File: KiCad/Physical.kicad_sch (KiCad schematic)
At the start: 11 parts, among them J159 Screw_Terminal_01x02, U106 AO3400A, U149 MT-0-103-F001-T000-RS+PJ, U181 AO3400A

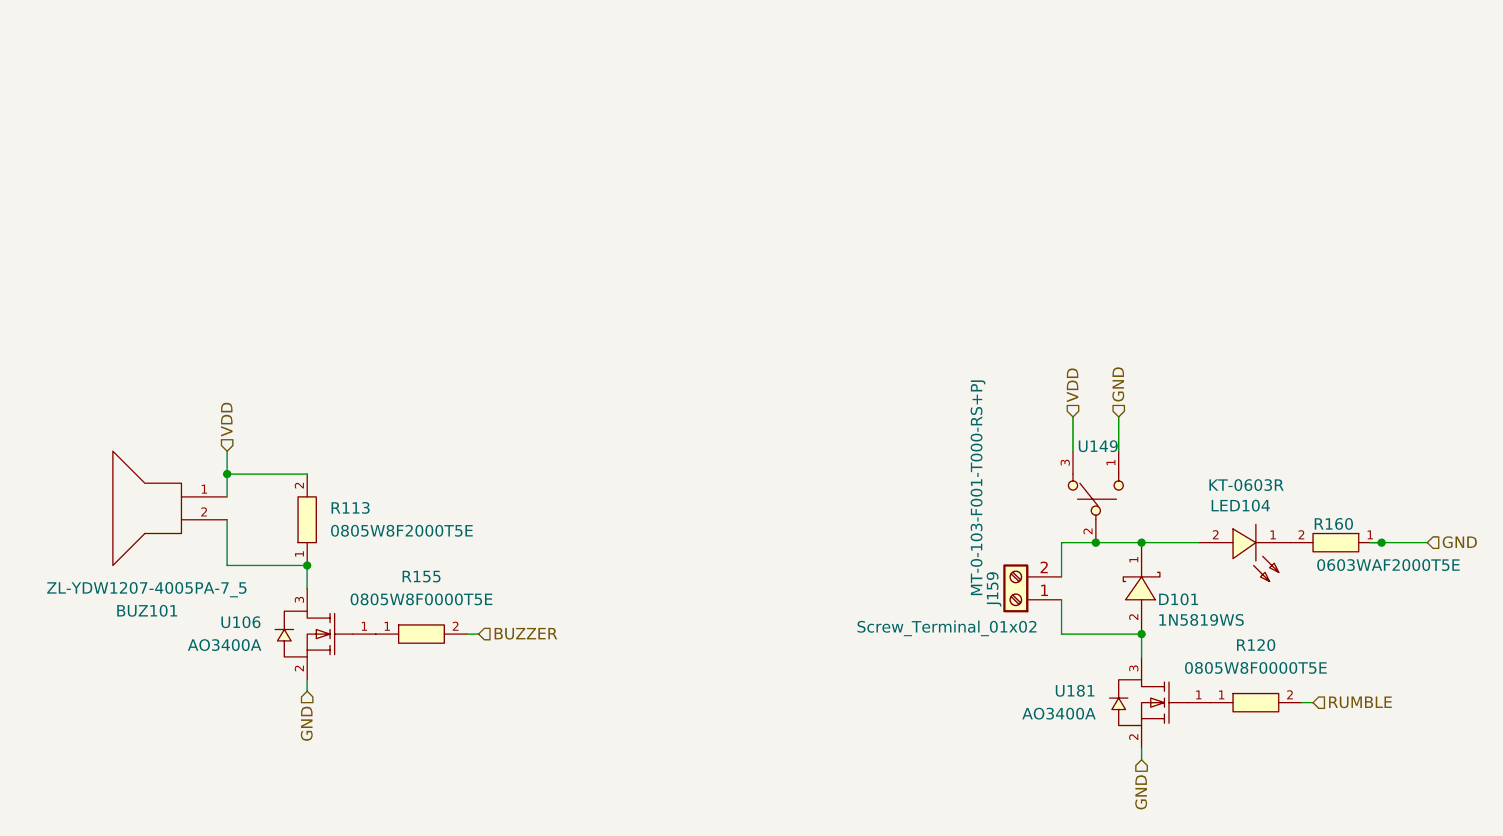
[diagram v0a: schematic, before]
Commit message: Updated to not use adressable LED. Sch only
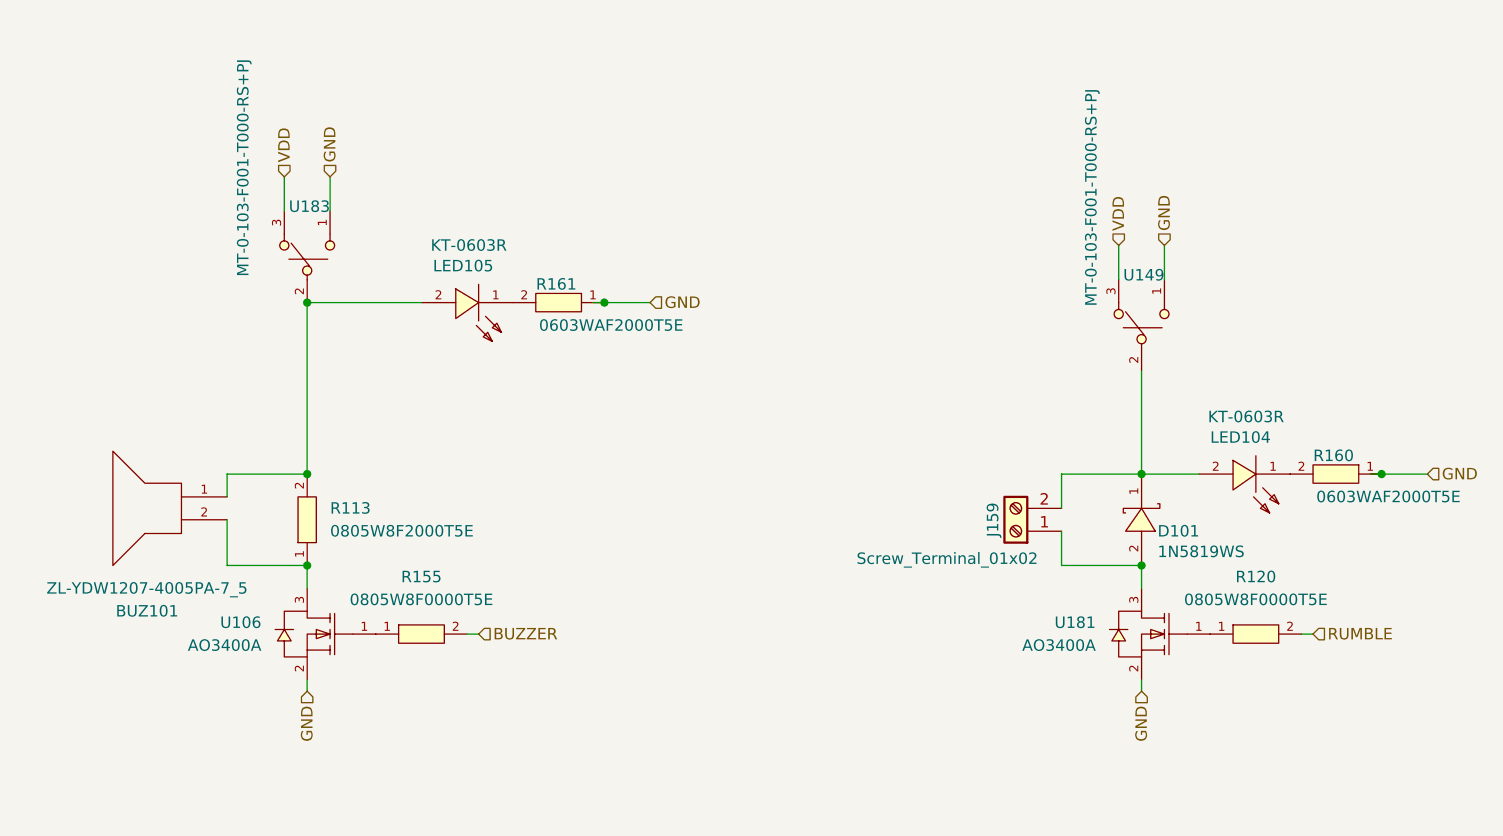
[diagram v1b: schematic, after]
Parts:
- added LED105: KT-0603R, footprint:LED0603-RD, symbol KT-0603R:KT-0603R
- added R161: 0603WAF2000T5E, footprint:R0603, symbol 0603WAF2000T5E:0603WAF2000T5E
- added U183: MT-0-103-F001-T000-RS+PJ, footprint:SW-TH_MT-0-103-A101-M200-RS, symbol MT-0-103-F001-T000-RS+PJ:MT-0-103-F001-T000-RS+PJ
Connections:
- net GND: now also R161.1, U183.1
- net VDD: now also U183.3; no longer BUZ101.1, R113.2
- new net: LED105.1 (K), R161.2
- new net: BUZ101.1, LED105.2 (A), R113.2, U183.2
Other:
- moved on the sheet: D101, J159, LED104, R120, R160, U149, U181

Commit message: Ready for PCB layout with discreet LEDs
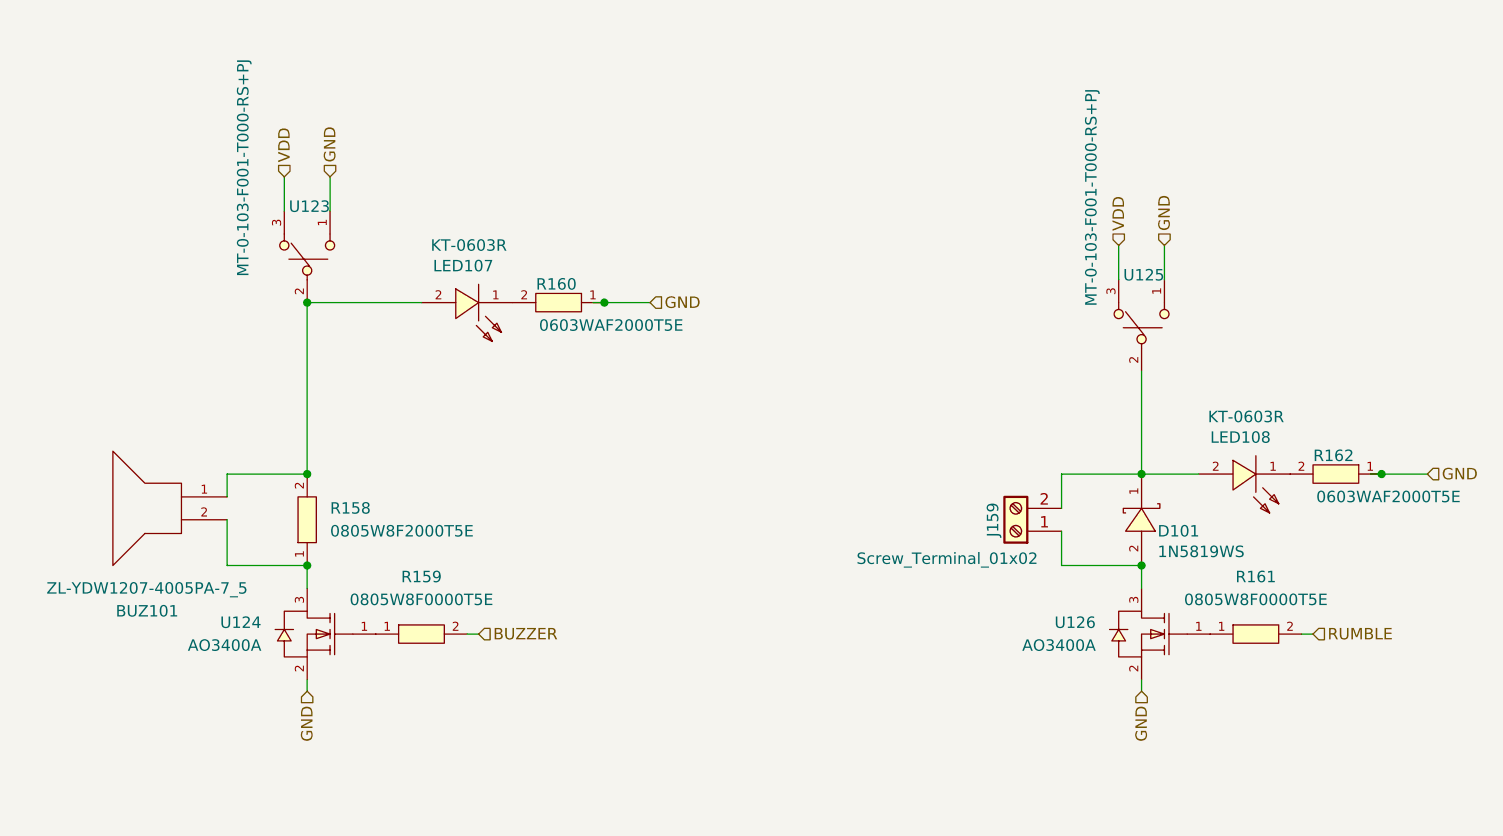
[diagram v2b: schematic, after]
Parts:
- renumbered LED105 to LED107, LED104 to LED108, R113 to R158, R155 to R159, R161 to R160, R120 to R161, R160 to R162, U183 to U123, U106 to U124, U149 to U125, U181 to U126
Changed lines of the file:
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@@
 		(on_board yes)
 		(dnp no)
-		(property "Reference" "R160"
+		(property "Reference" "R162"
 			(at 205.486 80.518 0)
 			(effects
@@
 			(project "Kaboom_box"
 				(path "/8d340784-229e-46d1-990c-7f8852f9fc49/d111de2c-3c3c-486e-8c4b-bd3963817676/683188d6-6efb-4f29-934c-2bc96d97ffe7"
-					(reference "R160")
+					(reference "R162")
 					(unit 1)
 				)
@@
 		(dnp no)
 		(fields_autoplaced yes)
-		(property "Reference" "R155"
+		(property "Reference" "R159"
 			(at 104.14 93.98 0)
 			(effects
@@
 			(project "Kaboom_box"
 				(path "/8d340784-229e-46d1-990c-7f8852f9fc49/d111de2c-3c3c-486e-8c4b-bd3963817676/683188d6-6efb-4f29-934c-2bc96d97ffe7"
-					(reference "R155")
+					(reference "R159")
 					(unit 1)
 				)
@@
 		(on_board yes)
 		(dnp no)
-		(property "Reference" "LED105"
+		(property "Reference" "LED107"
 			(at 105.41 59.436 0)
 			(effects
@@
 			(project "Kaboom_box"
 				(path "/8d340784-229e-46d1-990c-7f8852f9fc49/d111de2c-3c3c-486e-8c4b-bd3963817676/683188d6-6efb-4f29-934c-2bc96d97ffe7"
-					(reference "LED105")
+					(reference "LED107")
 					(unit 1)
 				)
@@
 		(dnp no)
 		(fields_autoplaced yes)
-		(property "Reference" "R120"
+		(property "Reference" "R161"
 			(at 196.85 93.98 0)
 			(effects
@@
 			(project "Kaboom_box"
 				(path "/8d340784-229e-46d1-990c-7f8852f9fc49/d111de2c-3c3c-486e-8c4b-bd3963817676/683188d6-6efb-4f29-934c-2bc96d97ffe7"
-					(reference "R120")
+					(reference "R161")
 					(unit 1)
 				)
@@
 		(on_board yes)
 		(dnp no)
-		(property "Reference" "U149"
+		(property "Reference" "U125"
 			(at 184.404 60.452 0)
 			(effects
@@
 			(project "Kaboom_box"
 				(path "/8d340784-229e-46d1-990c-7f8852f9fc49/d111de2c-3c3c-486e-8c4b-bd3963817676/683188d6-6efb-4f29-934c-2bc96d97ffe7"
-					(reference "U149")
+					(reference "U125")
 					(unit 1)
 				)
@@
 		(on_board yes)
 		(dnp no)
-		(property "Reference" "LED104"
+		(property "Reference" "LED108"
 			(at 191.77 78.486 0)
 			(effects
@@
 			(project "Kaboom_box"
 				(path "/8d340784-229e-46d1-990c-7f8852f9fc49/d111de2c-3c3c-486e-8c4b-bd3963817676/683188d6-6efb-4f29-934c-2bc96d97ffe7"
-					(reference "LED104")
+					(reference "LED108")
 					(unit 1)
 				)
@@
 		(dnp no)
 		(fields_autoplaced yes)
-		(property "Reference" "R113"
+		(property "Reference" "R158"
 			(at 93.98 86.36 90)
 			(effects
@@
 			(project "Kaboom_box"
 				(path "/8d340784-229e-46d1-990c-7f8852f9fc49/d111de2c-3c3c-486e-8c4b-bd3963817676/683188d6-6efb-4f29-934c-2bc96d97ffe7"
-					(reference "R113")
+					(reference "R158")
 					(unit 1)
 				)
@@
 		(on_board yes)
 		(dnp no)
-		(property "Reference" "U183"
+		(property "Reference" "U123"
 			(at 91.694 52.832 0)
 			(effects
@@
 			(project "Kaboom_box"
 				(path "/8d340784-229e-46d1-990c-7f8852f9fc49/d111de2c-3c3c-486e-8c4b-bd3963817676/683188d6-6efb-4f29-934c-2bc96d97ffe7"
-					(reference "U183")
+					(reference "U123")
 					(unit 1)
 				)
@@
 		(dnp no)
 		(fields_autoplaced yes)
-		(property "Reference" "U106"
+		(property "Reference" "U124"
 			(at 86.36 99.06 0)
 			(effects
@@
 			(project "Kaboom_box"
 				(path "/8d340784-229e-46d1-990c-7f8852f9fc49/d111de2c-3c3c-486e-8c4b-bd3963817676/683188d6-6efb-4f29-934c-2bc96d97ffe7"
-					(reference "U106")
+					(reference "U124")
 					(unit 1)
 				)
@@
 		(on_board yes)
 		(dnp no)
-		(property "Reference" "R161"
+		(property "Reference" "R160"
 			(at 119.126 61.468 0)
 			(effects
@@
 			(project "Kaboom_box"
 				(path "/8d340784-229e-46d1-990c-7f8852f9fc49/d111de2c-3c3c-486e-8c4b-bd3963817676/683188d6-6efb-4f29-934c-2bc96d97ffe7"
-					(reference "R161")
+					(reference "R160")
 					(unit 1)
 				)
@@
 		(dnp no)
 		(fields_autoplaced yes)
-		(property "Reference" "U181"
+		(property "Reference" "U126"
 			(at 179.07 99.06 0)
 			(effects
@@
 			(project "Kaboom_box"
 				(path "/8d340784-229e-46d1-990c-7f8852f9fc49/d111de2c-3c3c-486e-8c4b-bd3963817676/683188d6-6efb-4f29-934c-2bc96d97ffe7"
-					(reference "U181")
-					(unit 1)
-				)
+					(reference "U126")
+					(unit 1)
+				)
